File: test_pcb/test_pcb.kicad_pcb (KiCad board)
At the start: 2 copper layers, 76 x 114 mm, 66 parts, among them K0 KEYSW, K1 KEYSW, K10 KEYSW, K12 KEYSW, K13 KEYSW, K14 KEYSW, K15 KEYSW, K16 KEYSW, K17 KEYSW, K18 KEYSW, K2 KEYSW, K20 KEYSW, K21 KEYSW, K22 KEYSW, K3 KEYSW, K4 KEYSW, K5 KEYSW, K6 KEYSW, K7 KEYSW, K8 KEYSW, K9 KEYSW, P0 CONN_01X08, U0 Teensy3.2, U1 STP16CP05

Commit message: updates?
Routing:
- net green0: track 149.5 -> 148.5 mm
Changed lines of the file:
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@@
     (thickness 1.6)
     (drawings 5)
-    (tracks 1460)
+    (tracks 1459)
     (zones 0)
     (modules 66)
@@
   (segment (start 114.96 140.92) (end 121.92 133.96) (width 0.25) (layer B.Cu) (net 88))
   (segment (start 82.04 140.92) (end 110.54 140.92) (width 0.25) (layer B.Cu) (net 88))
-  (segment (start 113.75 86.75) (end 113.75 87) (width 0.25) (layer B.Cu) (net 89))
+  (segment (start 114.25 87.5) (end 114.25 78) (width 0.25) (layer B.Cu) (net 89))
+  (segment (start 114.25 76.75) (end 113.75 76.25) (width 0.25) (layer F.Cu) (net 89))
+  (segment (start 114.25 77) (end 114.25 76.75) (width 0.25) (layer F.Cu) (net 89))
+  (segment (start 114.25 78) (end 114.25 77) (width 0.25) (layer F.Cu) (net 89))
+  (via (at 114.25 78) (size 0.6) (drill 0.4) (layers F.Cu B.Cu) (net 89))
   (via (at 116.75 90) (size 0.6) (drill 0.4) (layers F.Cu B.Cu) (net 89))
-  (segment (start 113.75 87) (end 116.75 90) (width 0.25) (layer B.Cu) (net 89))
+  (segment (start 114.25 87.5) (end 116.75 90) (width 0.25) (layer B.Cu) (net 89))
   (segment (start 105.25 58.5) (end 95.25 58.5) (width 0.25) (layer F.Cu) (net 89))
   (segment (start 107.75 55.5) (end 107.5 55.75) (width 0.25) (layer F.Cu) (net 89))
@@
   (segment (start 125 55.5) (end 124.75 55.75) (width 0.25) (layer F.Cu) (net 89))
   (segment (start 124.75 57.75) (end 124 58.5) (width 0.25) (layer F.Cu) (net 89))
-  (segment (start 113.75 86) (end 113.75 86.75) (width 0.25) (layer B.Cu) (net 89))
   (segment (start 111.5 74.5) (end 112 74.5) (width 0.25) (layer F.Cu) (net 89))
-  (segment (start 112 74.5) (end 113.75 76.25) (width 0.25) (layer F.Cu) (net 89))
   (segment (start 111.5 74.5) (end 109.525 74.5) (width 0.25) (layer F.Cu) (net 89))
-  (via (at 113.75 78) (size 0.6) (drill 0.4) (layers F.Cu B.Cu) (net 89))
-  (segment (start 113.75 78) (end 113.75 86) (width 0.25) (layer B.Cu) (net 89))
-  (segment (start 113.75 76.25) (end 113.75 78) (width 0.25) (layer F.Cu) (net 89))
+  (segment (start 112 74.5) (end 113.75 76.25) (width 0.25) (layer F.Cu) (net 89))
   (segment (start 70.75 66.5) (end 70.5 66.25) (width 0.25) (layer B.Cu) (net 89))
   (segment (start 70.5 61) (end 70.75 60.75) (width 0.25) (layer B.Cu) (net 89))
@@
   (segment (start 122 119.25) (end 134 107.25) (width 0.25) (layer F.Cu) (net 91))
   (segment (start 131.5 134.975) (end 131.5 134.25) (width 0.25) (layer F.Cu) (net 91))
+  (segment (start 112.5 88.5) (end 117 93) (width 0.25) (layer B.Cu) (net 92))
   (segment (start 120 92.25) (end 119.25 93) (width 0.25) (layer B.Cu) (net 92))
-  (segment (start 119.25 93) (end 115.25 93) (width 0.25) (layer B.Cu) (net 92))
-  (segment (start 115.25 93) (end 112.5 90.25) (width 0.25) (layer B.Cu) (net 92))
-  (segment (start 120.325 91.925) (end 121.15 91.925) (width 0.25) (layer B.Cu) (net 92))
   (segment (start 120.325 91.925) (end 120 92.25) (width 0.25) (layer B.Cu) (net 92))
+  (segment (start 120.325 91.925) (end 121.15 91.925) (width 0.25) (layer B.Cu) (net 92))
+  (segment (start 119.25 93) (end 117 93) (width 0.25) (layer B.Cu) (net 92))
   (segment (start 113.75 73.25) (end 113.75 70) (width 0.25) (layer B.Cu) (net 92))
   (via (at 113.75 70) (size 0.6) (drill 0.4) (layers F.Cu B.Cu) (net 92))
@@
   (segment (start 111.5 75.5) (end 112 76) (width 0.25) (layer B.Cu) (net 92))
   (segment (start 112 76) (end 112.5 76.5) (width 0.25) (layer B.Cu) (net 92))
-  (segment (start 112.5 76.5) (end 112.5 90.25) (width 0.25) (layer B.Cu) (net 92))
+  (segment (start 112.5 76.5) (end 112.5 88.5) (width 0.25) (layer B.Cu) (net 92))
   (via (at 111.5 75.5) (size 0.6) (drill 0.4) (layers F.Cu B.Cu) (net 92))
   (segment (start 110.75 75.5) (end 111.5 75.5) (width 0.25) (layer F.Cu) (net 92))
@@
   (segment (start 72 75.75) (end 71.525 75.55) (width 0.25) (layer F.Cu) (net 92))
   (segment (start 90.525 75.55) (end 90.2 75.55) (width 0.25) (layer F.Cu) (net 92))
+  (via (at 115.75 86) (size 0.6) (drill 0.4) (layers F.Cu B.Cu) (net 93))
+  (segment (start 115 76.25) (end 115.75 77) (width 0.25) (layer F.Cu) (net 93))
+  (via (at 115.75 77) (size 0.6) (drill 0.4) (layers F.Cu B.Cu) (net 93))
+  (segment (start 115.75 77) (end 115.75 86) (width 0.25) (layer B.Cu) (net 93))
   (segment (start 107 55.25) (end 107 57.25) (width 0.25) (layer F.Cu) (net 93))
   (segment (start 107.8 54.45) (end 107 55.25) (width 0.25) (layer F.Cu) (net 93))
@@
   (segment (start 126.025 54.45) (end 124.8 54.45) (width 0.25) (layer F.Cu) (net 93))
   (segment (start 124.25 57.5) (end 123.75 58) (width 0.25) (layer F.Cu) (net 93))
-  (segment (start 115 83) (end 115 85.25) (width 0.25) (layer B.Cu) (net 93))
   (segment (start 116.5 86.75) (end 117.25 86.75) (width 0.25) (layer F.Cu) (net 93))
-  (segment (start 115 85.25) (end 116.5 86.75) (width 0.25) (layer F.Cu) (net 93))
-  (via (at 115 85.25) (size 0.6) (drill 0.4) (layers F.Cu B.Cu) (net 93))
+  (segment (start 115.75 86) (end 116.5 86.75) (width 0.25) (layer F.Cu) (net 93))
   (segment (start 118.5 86.75) (end 119.25 86.75) (width 0.25) (layer B.Cu) (net 93))
   (segment (start 120.525 88.025) (end 120.25 87.75) (width 0.25) (layer B.Cu) (net 93))
@@
   (segment (start 118.5 86.75) (end 117.25 86.75) (width 0.25) (layer F.Cu) (net 93))
   (segment (start 119.25 86.75) (end 120 87.5) (width 0.25) (layer B.Cu) (net 93))
-  (segment (start 115 76.25) (end 115 79.5) (width 0.25) (layer F.Cu) (net 93))
-  (segment (start 115 79.5) (end 115 83) (width 0.25) (layer B.Cu) (net 93))
-  (via (at 115 79.5) (size 0.6) (drill 0.4) (layers F.Cu B.Cu) (net 93))
   (segment (start 109.525 73.45) (end 112.2 73.45) (width 0.25) (layer F.Cu) (net 93))
   (segment (start 112.2 73.45) (end 115 76.25) (width 0.25) (layer F.Cu) (net 93))
@@
   (segment (start 88.25 77.5) (end 85 77.5) (width 0.25) (layer F.Cu) (net 93))
   (segment (start 90.525 73.45) (end 89.55 73.45) (width 0.25) (layer F.Cu) (net 93))
+  (segment (start 112.25 94) (end 114.75 94) (width 0.25) (layer F.Cu) (net 94))
+  (segment (start 114.75 94) (end 117.25 91.5) (width 0.25) (layer F.Cu) (net 94))
   (segment (start 119 92.75) (end 117.75 91.5) (width 0.25) (layer F.Cu) (net 94))
-  (segment (start 114.75 91.5) (end 113.5 92.75) (width 0.25) (layer F.Cu) (net 94))
-  (segment (start 117.75 91.5) (end 114.75 91.5) (width 0.25) (layer F.Cu) (net 94))
   (segment (start 120.25 94) (end 119 92.75) (width 0.25) (layer F.Cu) (net 94))
-  (segment (start 113.5 92.75) (end 112.25 94) (width 0.25) (layer F.Cu) (net 94))
+  (segment (start 117.75 91.5) (end 117.25 91.5) (width 0.25) (layer F.Cu) (net 94))
   (segment (start 110.45 94.55) (end 110.5 94.5) (width 0.25) (layer F.Cu) (net 94))
   (segment (start 109.525 94.55) (end 110.45 94.55) (width 0.25) (layer F.Cu) (net 94))

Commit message: test output holes
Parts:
- added P1: CONN_01X08, Socket_Strips:Socket_Strip_Straight_1x08_Pitch2.54mm, F.Cu at (135.0, 110.8)
- added P2: CONN_01X08, Socket_Strips:Socket_Strip_Straight_1x08_Pitch2.54mm, F.Cu at (135.0, 48.8)
- added R0, R1, R2: R, Resistors_SMD:R_0603_HandSoldering, F.Cu at (98.5, 165.6)
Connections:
- net Net-(U1-Pad24) renamed +3V3
- U1 pad 15: red2 -> Net-(R2-Pad2)
- U1 pad 16: red1 -> Net-(R1-Pad2)
- U1 pad 17: red0 -> Net-(R0-Pad2)
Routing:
- net Net-(P2-Pad8): track 0.00 -> 10.3 mm
- net Net-(R2-Pad2): track 0.00 -> 5.70 mm
- net red2: track 212.3 -> 206.6 mm
- net red0: track 157.2 -> 152.7 mm, vias 5 -> 4
- net Net-(R0-Pad2): track 0.00 -> 4.44 mm, vias 0 -> 1
- net red1: track 161.1 -> 157.8 mm
- net Net-(R1-Pad2): track 0.00 -> 2.03 mm
- net blue1: track 164.3 -> 163.0 mm

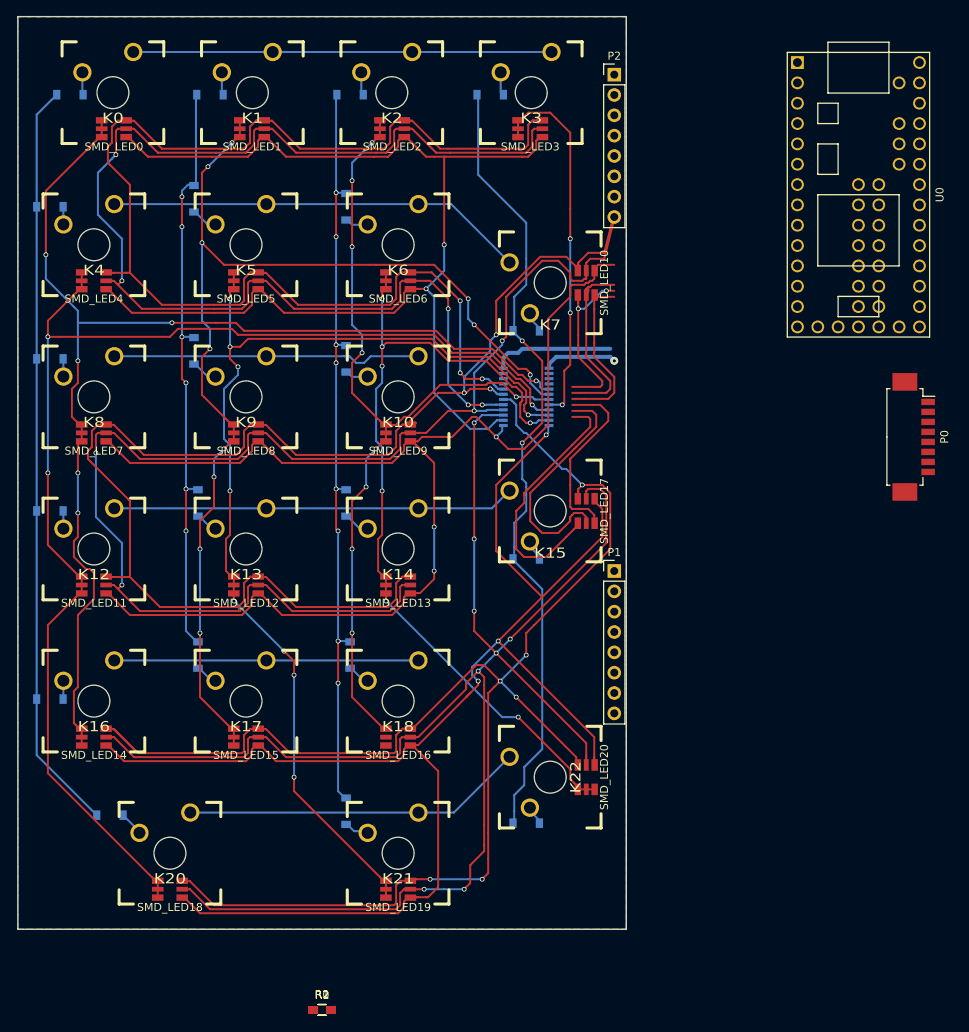
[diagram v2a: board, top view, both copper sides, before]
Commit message: test pcb freerouting is bugged on this right now
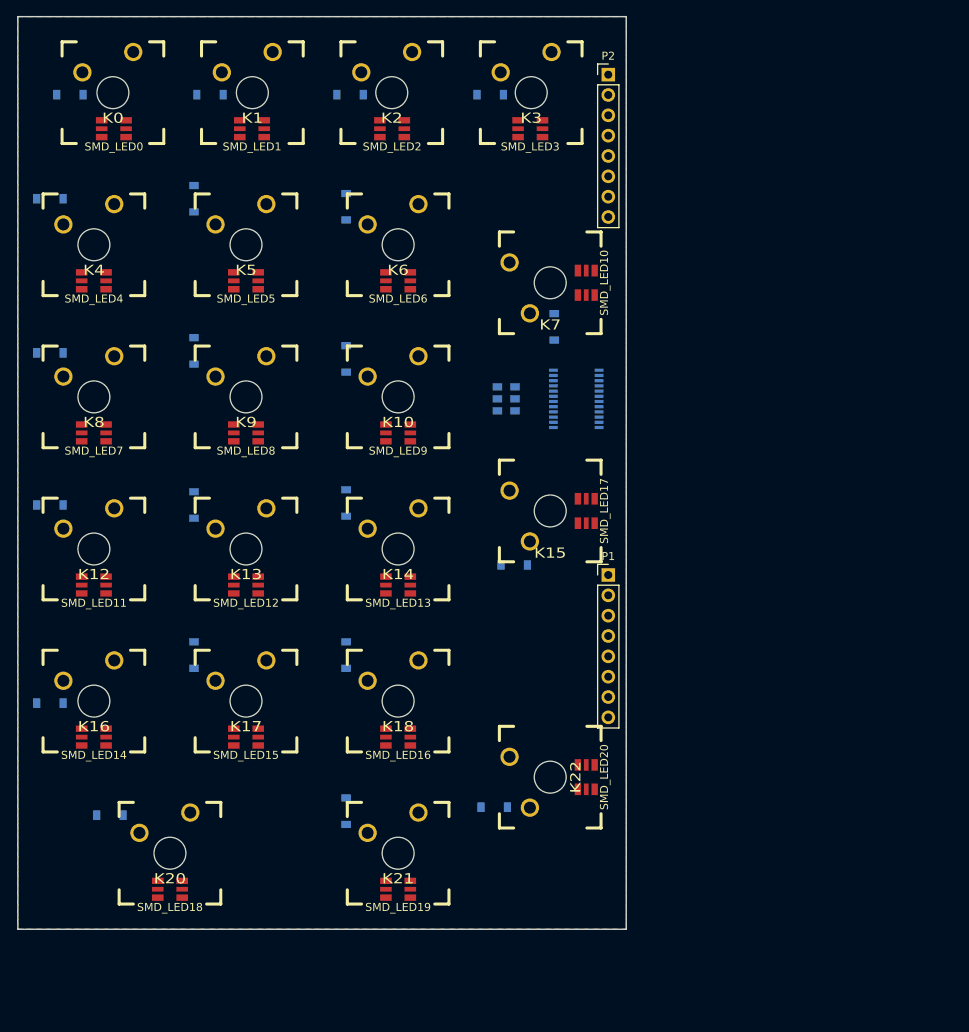
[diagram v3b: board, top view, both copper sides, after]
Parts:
- removed P0: CONN_01X08, Connectors_Molex:Molex_PicoBlade_53261-0871_08x1.25mm_Angled
- removed U0: Teensy3.2, Teensy:Teensy30_31_32_LC
- R0, R1, R2: moved to B.Cu
- moved R0 81.2 mm to (121.5, 87.8)
- moved R1 79.7 mm to (121.5, 89.2)
- moved R2 78.3 mm to (121.5, 90.8)
- moved U1 6.25 mm to (130.2, 89.2)
- moved D22 4.47 mm to (120.0, 140.2)
- moved D7 3.54 mm to (127.5, 80.2), turned to 90 degrees
- moved D15 1.68 mm to (122.5, 110.0)
- moved D4 1.00 mm to (64.5, 64.2)
- moved P1 0.90 mm to (134.2, 111.2)
- moved D12 0.75 mm to (64.5, 102.5)
- moved D8 0.75 mm to (64.5, 83.5)
- moved P2 0.75 mm to (134.2, 48.8)
- moved D13 0.56 mm to (82.5, 102.5)
- moved D16 0.50 mm to (64.5, 127.2)
- moved D17 0.50 mm to (82.5, 121.2)
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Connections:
- P2 pad 4: Net-(P2-Pad4) -> (no net)
- P2 pad 5: Net-(P2-Pad5) -> (no net)
- P2 pad 6: Net-(P2-Pad6) -> (no net)
- P2 pad 7: Net-(P2-Pad7) -> (no net)
- P2 pad 8: Net-(P2-Pad8) -> (no net)
- U1 pad 2: Net-(U1-Pad2) -> (no net)
- U1 pad 21: Net-(U1-Pad21) -> (no net)
- U1 pad 22: Net-(U1-Pad22) -> (no net)
- U1 pad 23: Net-(U1-Pad23) -> (no net)
- U1 pad 24: +3V3 -> (no net)
- U1 pad 3: Net-(U1-Pad3) -> (no net)
- U1 pad 4: Net-(U1-Pad4) -> (no net)
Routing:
- net red2: track 206.6 -> 0.00 mm, vias 8 -> 0
- net blue2: track 197.3 -> 0.00 mm, vias 6 -> 0
- net green2: track 188.5 -> 0.00 mm, vias 3 -> 0
- net blue1: track 163.0 -> 0.00 mm, vias 3 -> 0
- net a4: track 160.0 -> 0.00 mm, vias 3 -> 0
- net blue0: track 158.2 -> 0.00 mm, vias 3 -> 0
- net green1: track 158.1 -> 0.00 mm, vias 3 -> 0
- net red1: track 157.8 -> 0.00 mm, vias 4 -> 0
- net red0: track 152.7 -> 0.00 mm, vias 4 -> 0
- net a0: track 152.0 -> 0.00 mm, vias 6 -> 0
- net green0: track 148.5 -> 0.00 mm, vias 2 -> 0
- net a1: track 143.5 -> 0.00 mm, vias 11 -> 0
- net a5: track 136.6 -> 0.00 mm, vias 9 -> 0
- net a6: track 110.0 -> 0.00 mm, vias 7 -> 0
- net a2: track 108.6 -> 0.00 mm, vias 9 -> 0
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
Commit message: test pcb some improvement, but still getting the infinite fails
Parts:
- added P3: CONN_01X06, Socket_Strips:Socket_Strip_Straight_1x06_Pitch2.54mm, F.Cu at (127.5, 113.8)
- SMD_LED0, SMD_LED1, SMD_LED11, SMD_LED12, SMD_LED13, SMD_LED14, SMD_LED15, SMD_LED16, SMD_LED18, SMD_LED19, SMD_LED2, SMD_LED20, SMD_LED3, SMD_LED4, SMD_LED5, SMD_LED6, SMD_LED7, SMD_LED8, SMD_LED9: value SMLVN6RGB -> SMLVN6RGB_CA; footprint cherry_rgb:SMLVN6RGB -> cherry_rgb:SMLVN6RGB_CA
- moved P1 31.0 mm to (134.5, 80.2)
- moved R0 5.00 mm to (117.5, 90.8)
- moved R2 5.00 mm to (117.5, 87.8)
- moved U1 4.25 mm to (126.0, 89.2), turned to 90 degrees
- moved R1 4.00 mm to (117.5, 89.2)
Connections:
- P2 pad 4: (no net) -> green2
- P2 pad 5: (no net) -> c0
- P2 pad 6: (no net) -> c1
- P2 pad 7: (no net) -> c2
- P2 pad 8: (no net) -> c3
- U1 pad 2: (no net) -> Net-(U1-Pad2)
- U1 pad 21: (no net) -> Net-(U1-Pad21)
- U1 pad 22: (no net) -> Net-(U1-Pad22)
- U1 pad 23: (no net) -> Net-(U1-Pad23)
- U1 pad 24: (no net) -> +3V3
- U1 pad 3: (no net) -> Net-(U1-Pad3)
- U1 pad 4: (no net) -> Net-(U1-Pad4)

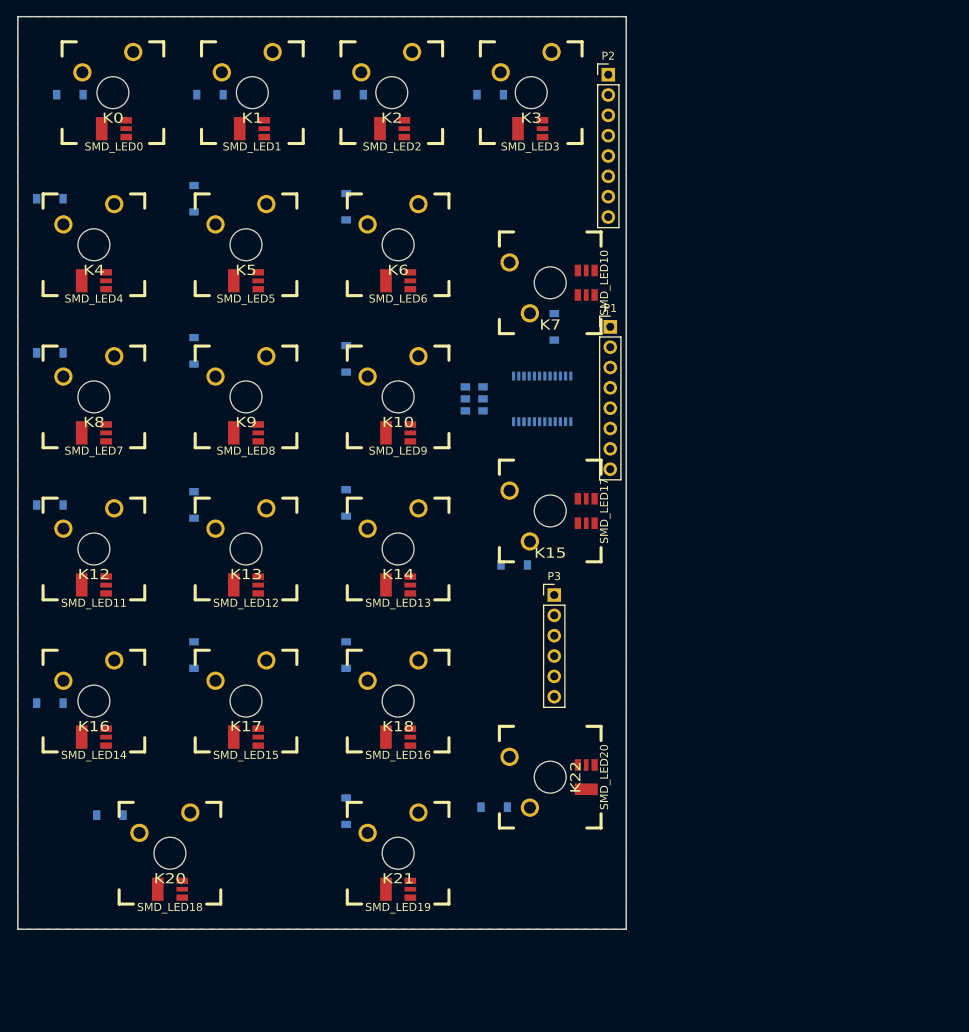
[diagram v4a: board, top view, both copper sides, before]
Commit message: test pcb seem to have fixed the routing bug
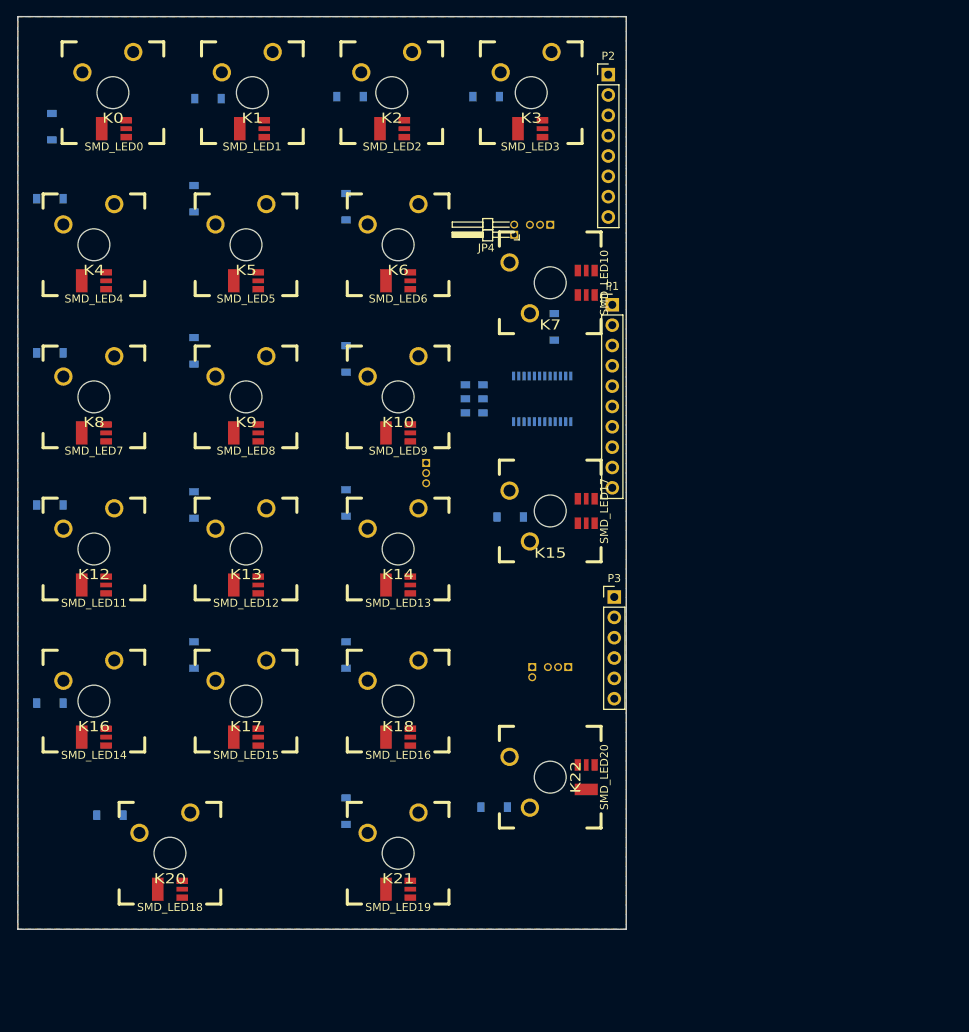
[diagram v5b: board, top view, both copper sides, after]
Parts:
- added JP1: Jumper_NC_Small, Pin_Headers:Pin_Header_Angled_1x02_Pitch1.27mm, B.Cu at (124.8, 122.8)
- added JP2: Jumper_NC_Dual, Pin_Headers:Pin_Header_Angled_1x03_Pitch1.27mm, B.Cu at (129.2, 122.8)
- added JP3: Jumper_NC_Dual, Pin_Headers:Pin_Header_Angled_1x03_Pitch1.27mm, B.Cu at (111.5, 97.2)
- added JP4: Jumper_NC_Small, Pin_Headers:Pin_Header_Angled_1x02_Pitch1.27mm, F.Cu at (122.5, 68.8)
- added JP5: Jumper_NC_Dual, Pin_Headers:Pin_Header_Angled_1x03_Pitch1.27mm, B.Cu at (127.0, 67.5)
- P1: value CONN_01X08 -> CONN_01X10; footprint Socket_Strips:Socket_Strip_Straight_1x08_Pitch2.54mm -> Socket_Strips:Socket_Strip_Straight_1x10_Pitch2.54mm
- moved P3 7.50 mm to (135.0, 114.0)
- moved D15 6.02 mm to (122.0, 104.0)
- moved D0 4.59 mm to (64.8, 55.2), turned to 90 degrees
- moved R0 3.25 mm to (117.5, 87.5)
- moved R2 3.25 mm to (117.5, 91.0)
- moved P1 2.76 mm to (134.8, 77.5)
- moved D1 0.56 mm to (84.2, 51.8)
- moved D3 0.56 mm to (119.0, 51.5)
- moved D2 0.25 mm to (102.0, 51.5)
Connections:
- P1 pad 1: a3-10-0 -> a3-10-2
- P1 pad 3: a3-10-2 -> a3-10-0
- P1 pad 4: a3-17-0 -> +3V3
- P1 pad 5: a3-17-1 -> GND
- P1 pad 6: a3-17-2 -> blue1
- P1 pad 7: blue1 -> red1
- P1 pad 8: red1 -> a3-17-0
- U1 pad 15: Net-(R2-Pad2) -> Net-(R0-Pad2)
- U1 pad 17: Net-(R0-Pad2) -> Net-(R2-Pad2)
- U1 pad 2: Net-(U1-Pad2) -> (no net)
- U1 pad 21: Net-(U1-Pad21) -> (no net)
- U1 pad 22: Net-(U1-Pad22) -> (no net)
- U1 pad 23: Net-(U1-Pad23) -> (no net)
- U1 pad 3: Net-(U1-Pad3) -> (no net)
- U1 pad 4: Net-(U1-Pad4) -> (no net)

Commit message: testp progress
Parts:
- added P10: CONN_01X01, Socket_Strips:Socket_Strip_Straight_1x01_Pitch1.27mm, F.Cu at (93.5, 88.2)
- added P11: CONN_01X01, Socket_Strips:Socket_Strip_Straight_1x01_Pitch1.27mm, F.Cu at (113.5, 70.5)
- added P12: CONN_01X01, Socket_Strips:Socket_Strip_Straight_1x01_Pitch1.27mm, F.Cu at (96.0, 60.2)
- added P13: CONN_01X01, Socket_Strips:Socket_Strip_Straight_1x01_Pitch1.27mm, F.Cu at (114.0, 77.0)
- added P14: CONN_01X01, Socket_Strips:Socket_Strip_Straight_1x01_Pitch1.27mm, F.Cu at (85.5, 100.8)
- added P15: CONN_01X01, Socket_Strips:Socket_Strip_Straight_1x01_Pitch1.27mm, F.Cu at (131.8, 83.8)
- added P4: CONN_01X01, Socket_Strips:Socket_Strip_Straight_1x01_Pitch1.27mm, F.Cu at (119.0, 114.2)
- added P5: CONN_01X01, Socket_Strips:Socket_Strip_Straight_1x01_Pitch1.27mm, F.Cu at (108.0, 116.2)
- added P6: CONN_01X01, Socket_Strips:Socket_Strip_Straight_1x01_Pitch1.27mm, F.Cu at (98.5, 114.2)
- added P7: CONN_01X01, Socket_Strips:Socket_Strip_Straight_1x01_Pitch1.27mm, F.Cu at (84.5, 116.2)
- added P8: CONN_01X01, Socket_Strips:Socket_Strip_Straight_1x01_Pitch1.27mm, F.Cu at (65.5, 116.2)
- added P9: CONN_01X01, Socket_Strips:Socket_Strip_Straight_1x01_Pitch1.27mm, F.Cu at (96.0, 79.2)
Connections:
- P1 pad 2: a3-10-1 -> a3-10-0
- P1 pad 3: a3-10-0 -> a3-10-1
- P2 pad 1: green1 -> r0
- P2 pad 2: blue2 -> r1
- P2 pad 3: red2 -> r2
- P2 pad 4: green2 -> green1
- P3 pad 1: r0 -> blue2
- P3 pad 2: r1 -> red2
- P3 pad 3: r2 -> green2
- U1 pad 10: a5 -> a4
- U1 pad 11: a6 -> a5
- U1 pad 12: green2 -> a6
- U1 pad 5: a0 -> green2
- U1 pad 6: a1 -> a0
- U1 pad 7: a2 -> a1
- U1 pad 8: a3 -> a2
- U1 pad 9: a4 -> a3
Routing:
- net red2: track 0.00 -> 187.3 mm, vias 0 -> 1
- net blue2: track 0.00 -> 172.3 mm, vias 0 -> 6
- net green0: track 0.00 -> 168.9 mm, vias 0 -> 6
- net c0: track 0.00 -> 167.8 mm
- net green2: track 0.00 -> 165.9 mm, vias 0 -> 2
- net green1: track 0.00 -> 163.4 mm, vias 0 -> 6
- net c1: track 0.00 -> 162.8 mm
- net red1: track 0.00 -> 161.7 mm, vias 0 -> 4
- net blue0: track 0.00 -> 157.7 mm, vias 0 -> 2
- net blue1: track 0.00 -> 154.7 mm, vias 0 -> 7
- net a0: track 0.00 -> 147.6 mm, vias 0 -> 1
- net red0: track 0.00 -> 143.1 mm, vias 0 -> 2
- net a4: track 0.00 -> 140.9 mm, vias 0 -> 1
- net c3: track 0.00 -> 131.0 mm, vias 0 -> 2
- net c2: track 0.00 -> 129.9 mm, vias 0 -> 5
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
